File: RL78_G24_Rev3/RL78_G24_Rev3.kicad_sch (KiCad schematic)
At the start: 45 parts, among them P1 POWER_JACKPTH, P2 E2 Lite, P3 Keypad, P5 F09HP, P6 SPI_to_eth, P7 LCD-1.8, P8 SD_Connector, U1 R7F101GB, U2 AMS1117-3.3, U3 MCP23008-E_P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

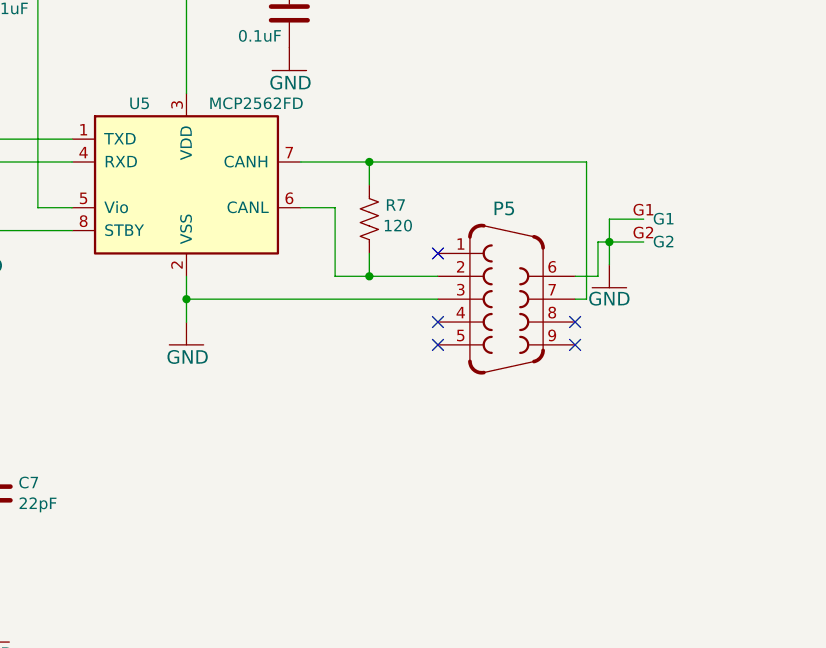
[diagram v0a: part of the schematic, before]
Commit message: Added RL78/F14 project and added jumper for the 120 ohms resistors in the G24 project
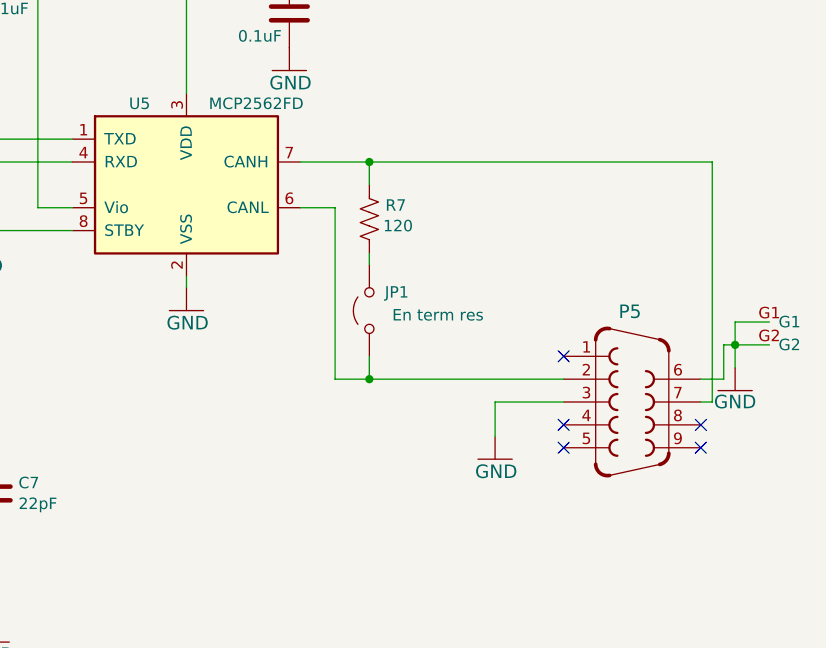
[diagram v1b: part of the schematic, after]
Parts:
- added JP1: En term res, Connector_PinHeader_2.54mm:PinHeader_1x02_P2.54mm_Vertical, symbol Jumper:Jumper_2_Open
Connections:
- net at P5.2, U5.6 (CANL): now also JP1.1 (A); no longer R7.2
- new net: JP1.2 (B), R7.2
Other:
- moved on the sheet: P5
